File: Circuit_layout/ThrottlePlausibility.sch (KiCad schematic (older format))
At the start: 63 parts, among them Q2 MMBF170, SW2 TS5A3159-Q1, U18 TS912, U2 MCP6002, U22 TS372, U23 TLP293, U24 TLP293, U3 MCP6004, U5 LM7810CT, U6 TS912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

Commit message: Completed errata changes
Committing before annotation, footprint assignment, and board relayout for backup purposes
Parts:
- removed C26: 0.1u, Capacitors_SMD:C_0805_HandSoldering, symbol C
- removed JP1: JUMPER3, Pin_Headers:Pin_Header_Straight_1x03_Pitch2.54mm, symbol JUMPER3
- removed R45, R47, R49, R53: 16k, Resistors_SMD:R_0805_HandSoldering, symbol R
- removed Thrtl_LPF1: Throttle_LPF, Measurement_Points:Measurement_Point_Round-SMD-Pad_Big, symbol TEST_1P
- removed Thrtl_uC1: Throttle_uC, Measurement_Points:Measurement_Point_Round-SMD-Pad_Big, symbol TEST_1P
- removed unit 2 of U2
- added APPS1_ISO?: APPS1_ISO, Measurement_Points:Measurement_Point_Round-SMD-Pad_Big, symbol TEST_1P
- added APPS_DIFF?: APPS_DIFF, Measurement_Points:Measurement_Point_Round-SMD-Pad_Big, symbol TEST_1P
- added RV? (x4): 2k, symbol POT_TRIM
- Q2: symbol MMBF170 -> MMBF170-RESCUE-Circuit_layout
- R25, R26: value 2k -> 4k
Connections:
- net APPS1_10: now also RV?.1; no longer R25.2
- net APPS1_ISO: now also APPS1_ISO?.1
- net GND: now also RV?.2, RV?.2, RV?.3, RV?.3; no longer R26.1, R34.1
- net Pedal_Out: now also SW2.1 (NO)
- net at R33.2, U22.3 (+): now also RV?.2, RV?.3; no longer R32.1
- net at R50.2, U18.7, U22.2 (-)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: now also APPS_DIFF?.1
- new net: R34.1, RV?.1
- new net: R32.1, RV?.1
- new net: R26.1, RV?.1
- new net: R25.2, RV?.2, RV?.3
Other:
- note removed: "Intended for 40kHz PWM\ntau=1.6ms"
- note removed: "uC Throttle PWM LPF"
- moved on the sheet: APPS1_b1, APPS2_b1, C16, C17, C22, C23, C38, C42, C43, C44, C45, Q2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

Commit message: Associated footprints and generated new netlist
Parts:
- RV1, RV2, RV3, RV4: renamed from RV?; footprint (none) -> custom_footprints:trim_pot
- gave numbers to parts that had none: 2

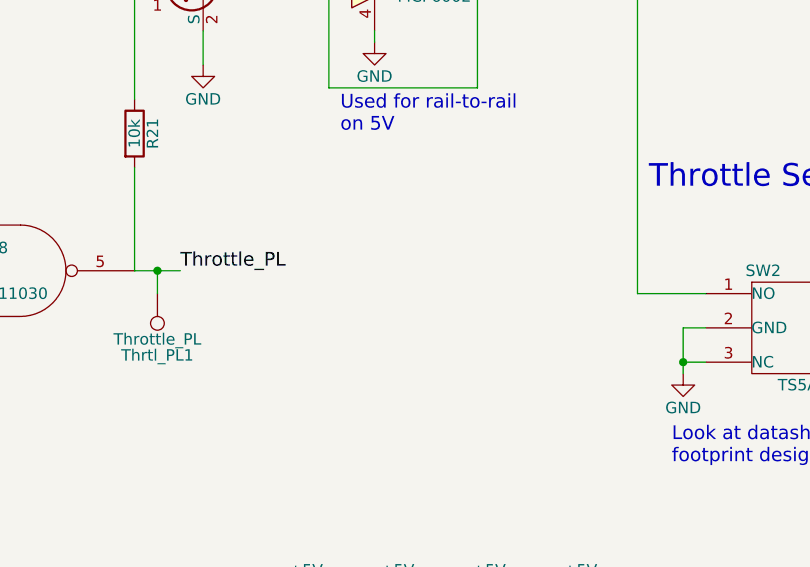
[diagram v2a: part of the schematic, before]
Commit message: Pots connected, just need to fit regulator on
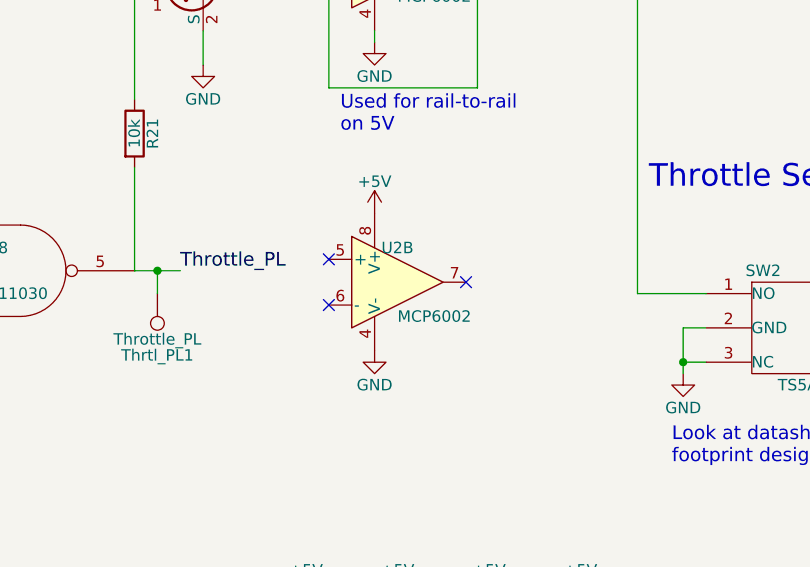
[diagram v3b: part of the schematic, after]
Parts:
- added unit 2 of U2
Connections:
- net +5V: now also U2.8 (V+)
- net GND: now also U2.4 (V-)
- no-connect marks 0 -> 3
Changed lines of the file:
@@
 Wire Wire Line
 	12800 8000 12800 8150
+$Comp
+L MCP6002 U2
+U 2 1 5A7D53DA
+P 12600 5300
+F 0 "U2" H 12600 5450 50  0000 C CNN
+F 1 "MCP6002" H 12600 5150 50  0000 L CNN
+F 2 "Housings_SOIC:SOIC-8_3.9x4.9mm_Pitch1.27mm" H 12500 5350 50  0001 C CNN
+F 3 "http://ww1.microchip.com/downloads/en/DeviceDoc/21733j.pdf" H 12600 5450 50  0001 C CNN
+F 4 "MCP6002T-I/SNCT-ND" H 12600 5300 60  0001 C CNN "DigiKey P/N"
+F 5 "http://www.digikey.com/product-detail/en/microchip-technology/MCP6002T-I-SN/MCP6002T-I-SNCT-ND/4307905" H 12600 5300 60  0001 C CNN "URL"
+F 6 "MCP6002T-I/SN" H 12600 5300 60  0001 C CNN "Man P/N"
+F 7 "IC OPAMP GP 1MHZ RRO 8SOIC" H 12600 5300 60  0001 C CNN "Description"
+F 8 "0.34" H 12600 5300 60  0001 C CNN "Cost"
+	2    12600 5300
+	1    0    0    -1
+$EndComp
+NoConn ~ 12900 5300
+NoConn ~ 12300 5200
+NoConn ~ 12300 5400
+$Comp
+L +5V #PWR0107
+U 1 1 5A7D5A7D
+P 12500 5000
+F 0 "#PWR0107" H 12500 4850 50  0001 C CNN
+F 1 "+5V" H 12500 5140 50  0000 C CNN
+F 2 "" H 12500 5000 50  0000 C CNN
+F 3 "" H 12500 5000 50  0000 C CNN
+	1    12500 5000
+	1    0    0    -1
+$EndComp
+$Comp
+L GND #PWR0108
+U 1 1 5A7D5B54
+P 12500 5600
+F 0 "#PWR0108" H 12500 5350 50  0001 C CNN
+F 1 "GND" H 12500 5450 50  0000 C CNN
+F 2 "" H 12500 5600 50  0000 C CNN
+F 3 "" H 12500 5600 50  0000 C CNN
+	1    12500 5600
+	1    0    0    -1
+$EndComp
 $EndSCHEMATC

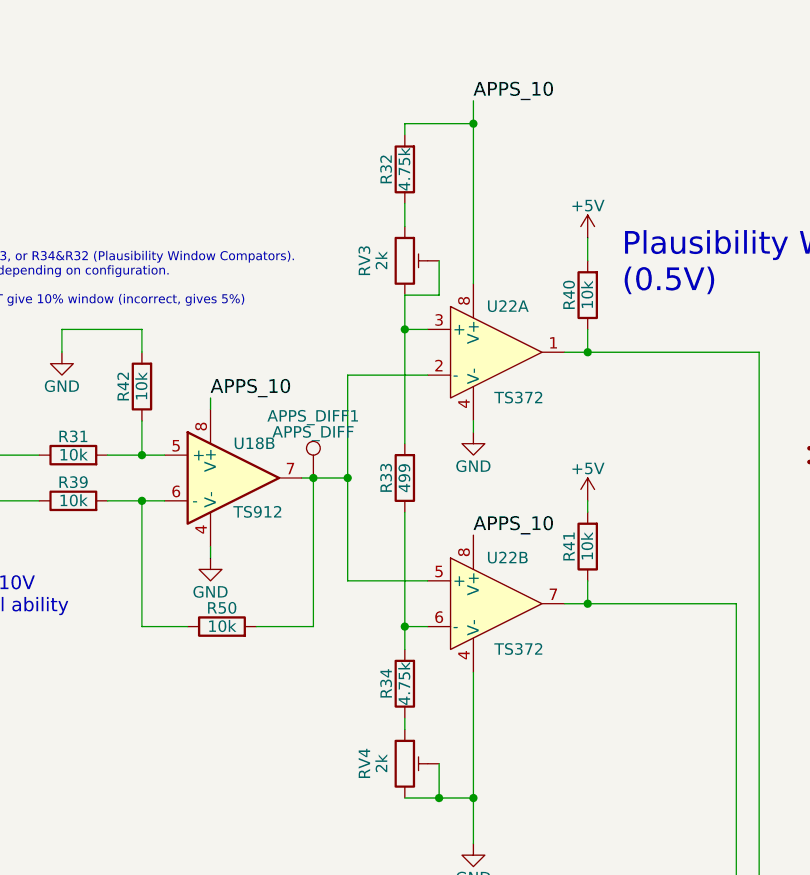
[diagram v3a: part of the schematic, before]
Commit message: Updated R32 and R34
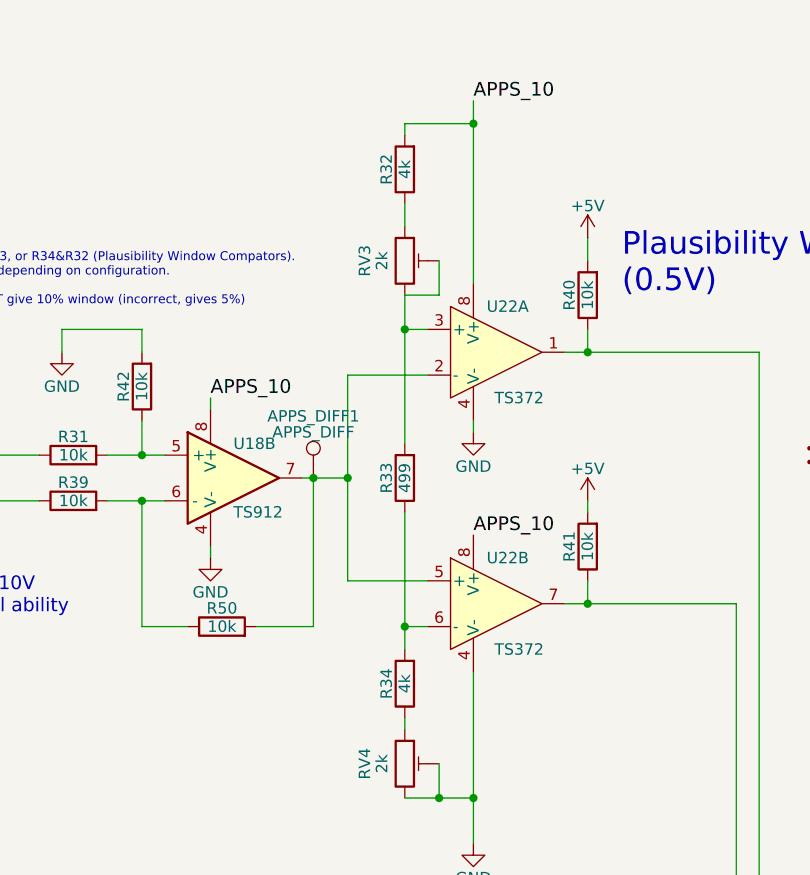
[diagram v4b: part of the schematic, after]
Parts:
- R32, R34: value 4.75k -> 4k
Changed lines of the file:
@@
 P 8500 3650
 F 0 "R34" V 8580 3650 50  0000 C CNN
-F 1 "4.75k" V 8500 3650 50  0000 C CNN
+F 1 "4k" V 8500 3650 50  0000 C CNN
 F 2 "Resistors_SMD:R_0805_HandSoldering" V 8430 3650 50  0001 C CNN
 F 3 "" H 8500 3650 50  0000 C CNN
@@
 P 8500 1400
 F 0 "R32" V 8580 1400 50  0000 C CNN
-F 1 "4.75k" V 8500 1400 50  0000 C CNN
+F 1 "4k" V 8500 1400 50  0000 C CNN
 F 2 "Resistors_SMD:R_0805_HandSoldering" V 8430 1400 50  0001 C CNN
 F 3 "" H 8500 1400 50  0000 C CNN

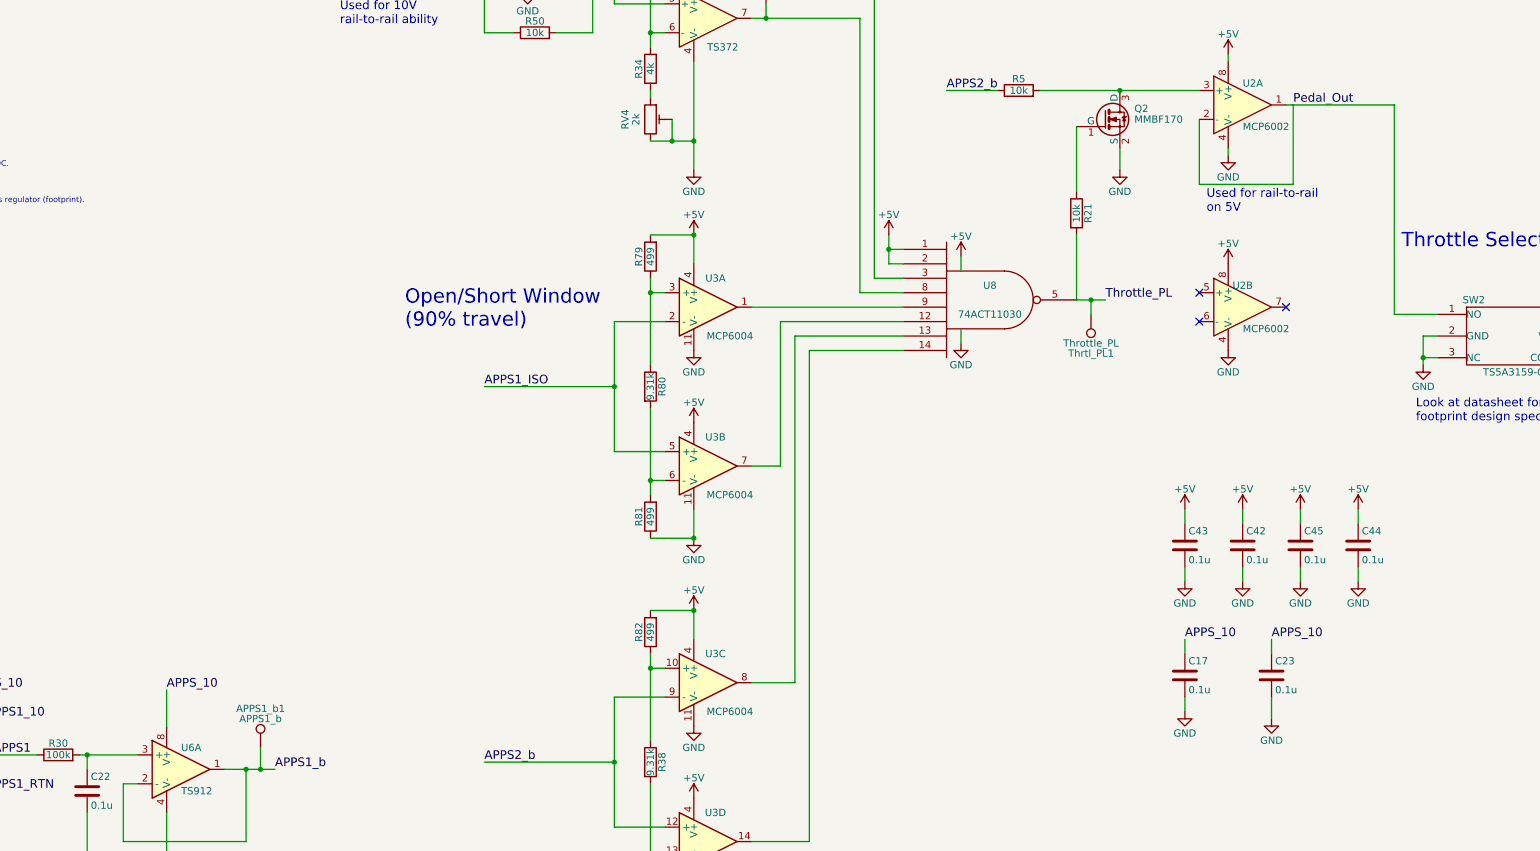
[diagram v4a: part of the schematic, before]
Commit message: Wider traces for DC/DC converter
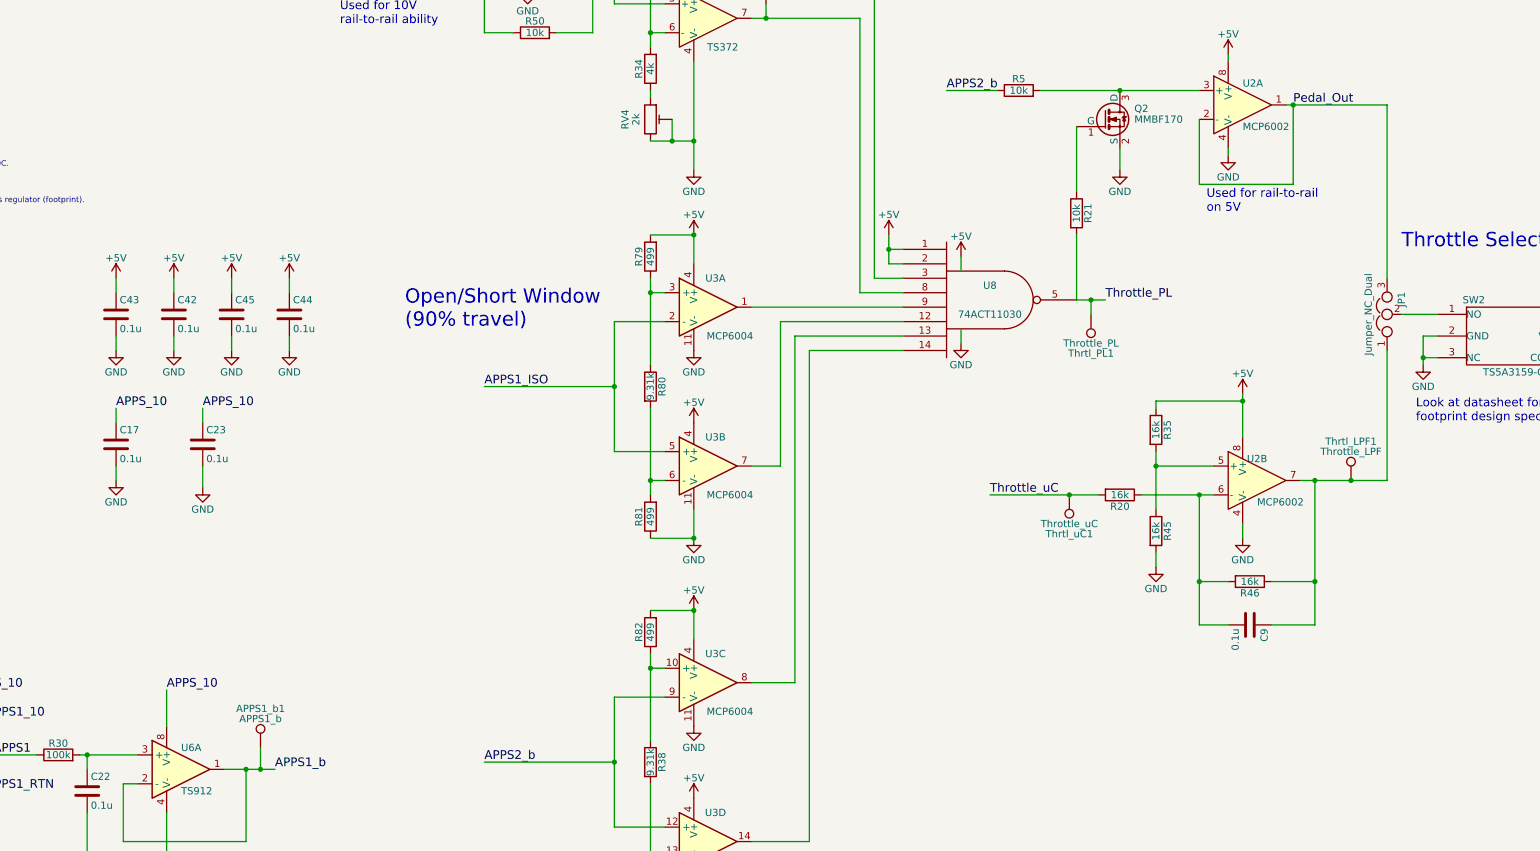
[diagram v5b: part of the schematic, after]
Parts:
- added C9: 0.1u, Capacitors_SMD:C_0805_HandSoldering, symbol C
- added JP1: Jumper_NC_Dual, Pin_Headers:Pin_Header_Straight_1x03_Pitch2.54mm, symbol Jumper_NC_Dual
- added R20, R35, R45, R46: 16k, Resistors_SMD:R_0805_HandSoldering, symbol R
- added Thrtl_LPF1: Throttle_LPF, Measurement_Points:Measurement_Point_Square-SMD-Pad_Big, symbol TEST_1P
- added Thrtl_uC1: Throttle_uC, Measurement_Points:Measurement_Point_Square-SMD-Pad_Big, symbol TEST_1P
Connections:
- net +5V: now also R35.1
- net GND: now also R45.2
- net Pedal_Out: now also JP1.3; no longer SW2.1 (NO)
- net Throttle_uC: now also R20.2, Thrtl_uC1.1
- net at U2.5 (+): now also R35.2, R45.1
- net at U2.6 (-): now also C9.2, R20.1, R46.2
- net at U2.7: now also C9.1, JP1.1, R46.1, Thrtl_LPF1.1
- new net: JP1.2, SW2.1 (NO)
- no-connect marks 3 -> 0
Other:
- moved on the sheet: C17, C23, C42, C43, C44, C45, U2B

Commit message: Generated gerber and drill files for board ordering
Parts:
- removed R52: 250k, Resistors_SMD:R_0805_HandSoldering, symbol R
- removed U24: TLP293, Housings_SSOP:SOP-4_4.4x2.8mm_Pitch1.27mm, symbol TLP291
- added D?: LED_ALT, symbol LED_ALT
- added R?: 1k, Resistors_SMD:R_0805_HandSoldering, symbol R
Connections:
- net GND: now also D?.1 (K)
- net Throttle_PL: now also R?.2
- new net: D?.2 (A), R?.1
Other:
- note added: "RED"
- note removed: "Brake Overtravel"

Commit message: Schematic update
Changed schematic to reflect board as assembeled
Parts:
- D5: renamed from D?; value LED_ALT -> ~Throttle_PL; footprint (none) -> LEDs:LED_0805
- gave numbers to parts that had none: 1
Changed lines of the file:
@@
 LIBS:ftdi
 LIBS:gennum
-LIBS:graphic
 LIBS:hc11
 LIBS:intel
@@
 LIBS:Lattice
 LIBS:linear
-LIBS:logo
 LIBS:maxim
 LIBS:memory
@@
 BOT_uC
 $Comp
-L GND #PWR096
+L GND #PWR095
 U 1 1 58C17F0F
 P 3800 9450
-F 0 "#PWR096" H 3800 9200 50  0001 C CNN
+F 0 "#PWR095" H 3800 9200 50  0001 C CNN
 F 1 "GND" H 3800 9300 50  0000 C CNN
 F 2 "" H 3800 9450 50  0000 C CNN
@@
 APPS_10
 $Comp
-L GND #PWR097
+L GND #PWR096
 U 1 1 58BFE2A1
 P 2550 9450
-F 0 "#PWR097" H 2550 9200 50  0001 C CNN
+F 0 "#PWR096" H 2550 9200 50  0001 C CNN
 F 1 "GND" H 2550 9300 50  0000 C CNN
 F 2 "" H 2550 9450 50  0000 C CNN
@@
 $EndComp
 $Comp
-L GND #PWR098
+L GND #PWR097
 U 1 1 58BFFFDF
 P 2000 9450
-F 0 "#PWR098" H 2000 9200 50  0001 C CNN
+F 0 "#PWR097" H 2000 9200 50  0001 C CNN
 F 1 "GND" H 2000 9300 50  0000 C CNN
 F 2 "" H 2000 9450 50  0000 C CNN
@@
 $EndComp
 $Comp
-L GND #PWR099
+L GND #PWR098
 U 1 1 58C09A9E
 P 5150 9450
-F 0 "#PWR099" H 5150 9200 50  0001 C CNN
+F 0 "#PWR098" H 5150 9200 50  0001 C CNN
 F 1 "GND" H 5150 9300 50  0000 C CNN
 F 2 "" H 5150 9450 50  0000 C CNN
@@
 $EndComp
 $Comp
-L GND #PWR0100
+L GND #PWR099
 U 1 1 58C09EB8
 P 4600 9450
-F 0 "#PWR0100" H 4600 9200 50  0001 C CNN
+F 0 "#PWR099" H 4600 9200 50  0001 C CNN
 F 1 "GND" H 4600 9300 50  0000 C CNN
 F 2 "" H 4600 9450 50  0000 C CNN
@@
 $EndComp
 $Comp
-L +24V #PWR0101
+L +24V #PWR0100
 U 1 1 58C0FB3A
 P 1350 3950
-F 0 "#PWR0101" H 1350 3800 50  0001 C CNN
+F 0 "#PWR0100" H 1350 3800 50  0001 C CNN
 F 1 "+24V" H 1350 4090 50  0000 C CNN
 F 2 "" H 1350 3950 50  0000 C CNN
@@
 APPS_10
 $Comp
-L GND #PWR0102
+L GND #PWR0101
 U 1 1 58C13EC3
 P 5400 6550
-F 0 "#PWR0102" H 5400 6300 50  0001 C CNN
+F 0 "#PWR0101" H 5400 6300 50  0001 C CNN
 F 1 "GND" H 5400 6400 50  0000 C CNN
 F 2 "" H 5400 6550 50  0000 C CNN
@@
 APPS1_b
 $Comp
-L GND #PWR0103
+L GND #PWR0102
 U 1 1 58C2062A
 P 2700 6250
-F 0 "#PWR0103" H 2700 6000 50  0001 C CNN
+F 0 "#PWR0102" H 2700 6000 50  0001 C CNN
 F 1 "GND" H 2700 6100 50  0000 C CNN
 F 2 "" H 2700 6250 50  0000 C CNN
@@
 $EndComp
 $Comp
-L GND #PWR0104
+L GND #PWR0103
 U 1 1 58C20630
 P 2200 6550
-F 0 "#PWR0104" H 2200 6300 50  0001 C CNN
+F 0 "#PWR0103" H 2200 6300 50  0001 C CNN
 F 1 "GND" H 2200 6400 50  0000 C CNN
 F 2 "" H 2200 6550 50  0000 C CNN
@@
 $EndComp
 $Comp
-L +5V #PWR0105
+L +5V #PWR0104
 U 1 1 58C2185C
 P 1150 5950
-F 0 "#PWR0105" H 1150 5800 50  0001 C CNN
+F 0 "#PWR0104" H 1150 5800 50  0001 C CNN
 F 1 "+5V" H 1150 6090 50  0000 C CNN
 F 2 "" H 1150 5950 50  0000 C CNN
@@
 $EndComp
 $Comp
-L GND #PWR0106
+L GND #PWR0105
 U 1 1 58C331D8
 P 12800 2550
-F 0 "#PWR0106" H 12800 2300 50  0001 C CNN
+F 0 "#PWR0105" H 12800 2300 50  0001 C CNN
 F 1 "GND" H 12800 2400 50  0000 C CNN
 F 2 "" H 12800 2550 50  0000 C CNN
@@
 Connection ~ 10150 4900
 $Comp
-L +5V #PWR0107
+L +5V #PWR0106
 U 1 1 58C55D3B
 P 10150 4800
-F 0 "#PWR0107" H 10150 4650 50  0001 C CNN
+F 0 "#PWR0106" H 10150 4650 50  0001 C CNN
 F 1 "+5V" H 10150 4940 50  0000 C CNN
 F 2 "" H 10150 4800 50  0000 C CNN
@@
 $EndComp
 $Comp
-L GND #PWR0108
+L GND #PWR0107
 U 1 1 58C5A996
 P 13850 5700
-F 0 "#PWR0108" H 13850 5450 50  0001 C CNN
+F 0 "#PWR0107" H 13850 5450 50  0001 C CNN
 F 1 "GND" H 13850 5550 50  0000 C CNN
 F 2 "" H 13850 5700 50  0000 C CNN
@@
 $EndComp
 $Comp
-L +5V #PWR0109
+L +5V #PWR0108
 U 1 1 58D04CF9
 P 15050 5200
-F 0 "#PWR0109" H 15050 5050 50  0001 C CNN
+F 0 "#PWR0108" H 15050 5050 50  0001 C CNN
 F 1 "+5V" H 15050 5340 50  0000 C CNN
 F 2 "" H 15050 5200 50  0000 C CNN
@@
 Look at datasheet for \nfootprint design specs
 $Comp
-L GND #PWR0110
+L GND #PWR0109
 U 1 1 58D1EB87
 P 10650 5550
-F 0 "#PWR0110" H 10650 5300 50  0001 C CNN
+F 0 "#PWR0109" H 10650 5300 50  0001 C CNN
 F 1 "GND" H 10650 5400 50  0000 C CNN
 F 2 "" H 10650 5550 50  0000 C CNN
@@
 	10650 5550 10650 5450
 $Comp
-L +5V #PWR0111
+L +5V #PWR0110
 U 1 1 58D1EDC9
 P 10650 4950
-F 0 "#PWR0111" H 10650 4800 50  0001 C CNN
+F 0 "#PWR0110" H 10650 4800 50  0001 C CNN
 F 1 "+5V" H 10650 5090 50  0000 C CNN
 F 2 "" H 10650 4950 50  0000 C CNN
@@
 $EndComp
 $Comp
-L +5V #PWR0112
+L +5V #PWR0111
 U 1 1 5A7D5A7D
 P 12600 5900
-F 0 "#PWR0112" H 12600 5750 50  0001 C CNN
+F 0 "#PWR0111" H 12600 5750 50  0001 C CNN
 F 1 "+5V" H 12600 6040 50  0000 C CNN
 F 2 "" H 12600 5900 50  0000 C CNN
@@
 $EndComp
 $Comp
-L GND #PWR0113
+L GND #PWR0112
 U 1 1 5A7D5B54
 P 12600 6900
-F 0 "#PWR0113" H 12600 6650 50  0001 C CNN
+F 0 "#PWR0112" H 12600 6650 50  0001 C CNN
 F 1 "GND" H 12600 6750 50  0000 C CNN
 F 2 "" H 12600 6900 50  0000 C CNN
@@
 $EndComp
 $Comp
-L GND #PWR0114
+L GND #PWR0113
 U 1 1 5A846229
 P 12000 7100
-F 0 "#PWR0114" H 12000 6850 50  0001 C CNN
+F 0 "#PWR0113" H 12000 6850 50  0001 C CNN
 F 1 "GND" H 12000 6950 50  0000 C CNN
 F 2 "" H 12000 7100 50  0000 C CNN
@@
 Connection ~ 13350 6500
 $Comp
-L R R?
+L R R47
 U 1 1 5A92FC89
 P 11250 8100
-F 0 "R?" V 11330 8100 50  0000 C CNN
+F 0 "R47" V 11330 8100 50  0000 C CNN
 F 1 "1k" V 11250 8100 50  0000 C CNN
 F 2 "Resistors_SMD:R_0805_HandSoldering" V 11180 8100 50  0001 C CNN
@@
 $EndComp
 $Comp
-L LED_ALT D?
+L LED_ALT D5
 U 1 1 5A9328C2
 P 11750 8100
-F 0 "D?" H 11750 8200 50  0000 C CNN
-F 1 "LED_ALT" H 11750 8000 50  0000 C CNN
-F 2 "" H 11750 8100 50  0001 C CNN
+F 0 "D5" H 11750 8200 50  0000 C CNN
+F 1 "~Throttle_PL" H 11750 7950 50  0000 C CNN
+F 2 "LEDs:LED_0805" H 11750 8100 50  0001 C CNN
 F 3 "" H 11750 8100 50  0001 C CNN
 	1    11750 8100
@@
 $EndComp
 $Comp
-L GND #PWR?
+L GND #PWR0114
 U 1 1 5A934199
 P 12000 8200
-F 0 "#PWR?" H 12000 7950 50  0001 C CNN
+F 0 "#PWR0114" H 12000 7950 50  0001 C CNN
 F 1 "GND" H 12000 8050 50  0000 C CNN
 F 2 "" H 12000 8200 50  0000 C CNN
